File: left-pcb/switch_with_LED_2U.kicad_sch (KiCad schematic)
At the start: 3 parts, among them SW6 SW_SPST

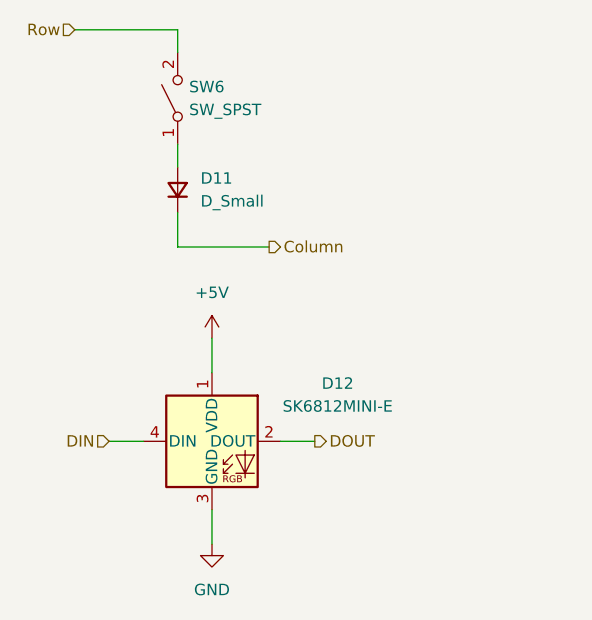
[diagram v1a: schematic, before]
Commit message: Initial modifications to reduce fab cost and add caps
Removing 1 row and column of keys, and majorly changing layout

Routing still in progress
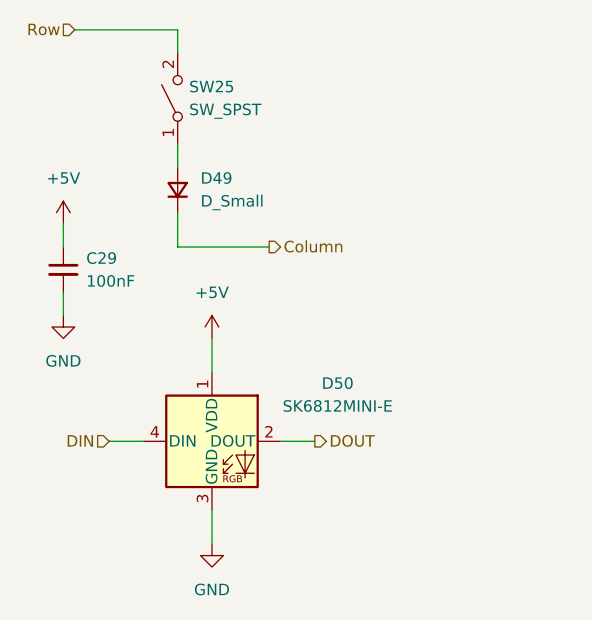
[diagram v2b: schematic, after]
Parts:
- removed D11: D_Small, Diode_SMD:D_SOD-123, symbol Device:D_Small
- removed D12: SK6812MINI-E, SW-Adafruit:LED_SK6812MINI-E_REVERSE_MOUNT_3.2x2.8mm_P1.09mm, symbol SW-Adafruit:SK6812MINI-E
- removed SW6: SW_SPST, PCM_Switch_Keyboard_Hotswap_Kailh:SW_Hotswap_Kailh_MX_2.00u, symbol Switch:SW_SPST
- added C29: 100nF, Capacitor_SMD:C_1206_3216Metric_Pad1.33x1.80mm_HandSolder, symbol Device:C_Small
- added D49: D_Small, Diode_SMD:D_SOD-123, symbol Device:D_Small
- added D50: SK6812MINI-E, SW-Adafruit:LED_SK6812MINI-E_REVERSE_MOUNT_3.2x2.8mm_P1.09mm, symbol SW-Adafruit:SK6812MINI-E
- added SW25: SW_SPST, PCM_Switch_Keyboard_Hotswap_Kailh:SW_Hotswap_Kailh_MX_2.00u, symbol Switch:SW_SPST
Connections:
- net +5V: now also C29.1, D50.1 (VDD)
- net Column: now also D49.1 (K)
- net DIN: now also D50.4 (DIN)
- net DOUT: now also D50.2 (DOUT)
- net GND: now also C29.2, D50.3 (GND)
- net Row: now also SW25.2 (B)
- new net: D49.2 (A), SW25.1 (A)

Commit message: Caps, shrunk board, added mounting holes
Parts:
- C29: footprint Capacitor_SMD:C_1206_3216Metric_Pad1.33x1.80mm_HandSolder -> Capacitor_SMD:C_0805_2012Metric_Pad1.18x1.45mm_HandSolder
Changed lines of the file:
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@@
 			)
 		)
-		(property "Footprint" "Capacitor_SMD:C_1206_3216Metric_Pad1.33x1.80mm_HandSolder"
+		(property "Footprint" "Capacitor_SMD:C_0805_2012Metric_Pad1.18x1.45mm_HandSolder"
 			(at 107.95 113.03 0)
 			(effects

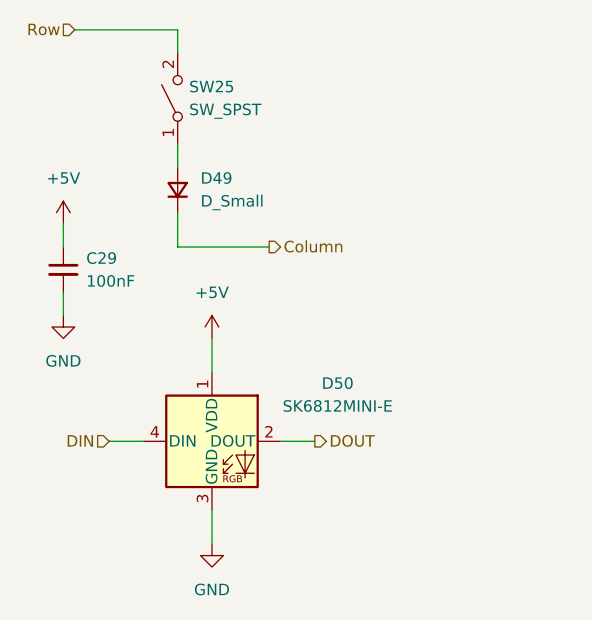
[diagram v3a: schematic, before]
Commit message: Adding values to Diodes and adding stabilizers to 2U switches
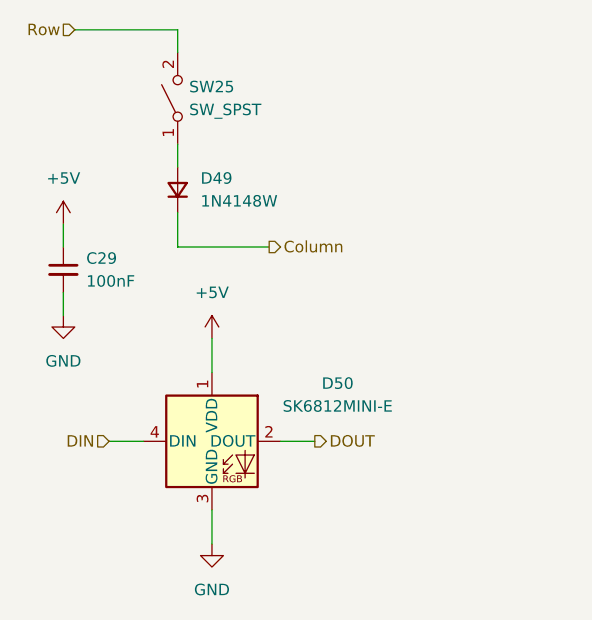
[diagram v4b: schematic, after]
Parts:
- D49: value D_Small -> 1N4148W
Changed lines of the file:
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@@
 			)
 		)
-		(property "Value" "D_Small"
+		(property "Value" "1N4148W"
 			(at 123.19 105.4099 90)
 			(effects

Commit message: Added extra column to left hand keyboard
Matching size to right hand side.
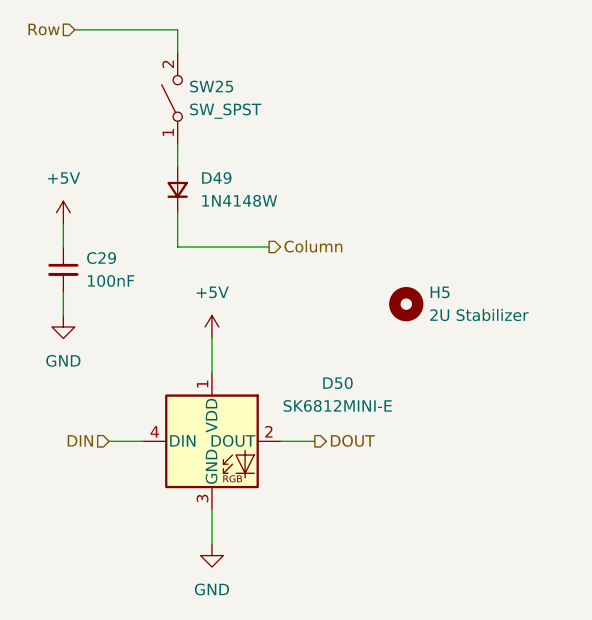
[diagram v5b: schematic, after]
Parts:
- added H5: 2U Stabilizer, PCM_Mounting_Keyboard_Stabilizer:Stabilizer_Cherry_MX_2.00u, symbol Mechanical:MountingHole
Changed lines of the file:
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@@
 		(dnp no)
 		(fields_autoplaced yes)
-		(property "Reference" "#PWR0113"
+		(property "Reference" "#PWR0114"
 			(at 107.95 124.46 0)
 			(effects
@@
 			(project "row_staggered_split_keyboard_left_side"
 				(path "/cf145565-22e2-4e5a-8a27-915862c57a1b/6b1ebd07-8927-4363-9ca1-15fd56b1bbda"
-					(reference "#PWR0113")
+					(reference "#PWR0114")
 					(unit 1)
 				)
@@
 		(dnp no)
 		(fields_autoplaced yes)
-		(property "Reference" "#PWR0114"
+		(property "Reference" "#PWR0115"
 			(at 124.46 124.46 0)
 			(effects
@@
 			(project "row_staggered_split_keyboard_left_side"
 				(path "/cf145565-22e2-4e5a-8a27-915862c57a1b/6b1ebd07-8927-4363-9ca1-15fd56b1bbda"
-					(reference "#PWR0114")
+					(reference "#PWR0115")
 					(unit 1)
 				)
@@
 		(dnp no)
 		(fields_autoplaced yes)
-		(property "Reference" "#PWR0115"
+		(property "Reference" "#PWR0116"
 			(at 124.46 149.86 0)
 			(effects
@@
 			(project "row_staggered_split_keyboard_left_side"
 				(path "/cf145565-22e2-4e5a-8a27-915862c57a1b/6b1ebd07-8927-4363-9ca1-15fd56b1bbda"
-					(reference "#PWR0115")
+					(reference "#PWR0116")
 					(unit 1)
 				)
@@
 	)
 	(symbol
+		(lib_id "Mechanical:MountingHole")
+		(at 146.05 116.84 0)
+		(unit 1)
+		(exclude_from_sim no)
+		(in_bom yes)
+		(on_board yes)
+		(dnp no)
+		(fields_autoplaced yes)
+		(property "Reference" "H5"
+			(at 148.59 115.5699 0)
+			(effects
+				(font
+					(size 1.27 1.27)
+				)
+				(justify left)
+			)
+		)
+		(property "Value" "2U Stabilizer"
+			(at 148.59 118.1099 0)
+			(effects
+				(font
+					(size 1.27 1.27)
+				)
+				(justify left)
+			)
+		)
+		(property "Footprint" "PCM_Mounting_Keyboard_Stabilizer:Stabilizer_Cherry_MX_2.00u"
+			(at 146.05 116.84 0)
+			(effects
+				(font
+					(size 1.27 1.27)
+				)
+				(hide yes)
+			)
+		)
+		(property "Datasheet" "~"
+			(at 146.05 116.84 0)
+			(effects
+				(font
+					(size 1.27 1.27)
+				)
+				(hide yes)
+			)
+		)
+		(property "Description" "Mounting Hole without connection"
+			(at 146.05 116.84 0)
+			(effects
+				(font
+					(size 1.27 1.27)
+				)
+				(hide yes)
+			)
+		)
+		(instances
+			(project ""
+				(path "/cf145565-22e2-4e5a-8a27-915862c57a1b/6b1ebd07-8927-4363-9ca1-15fd56b1bbda"
+					(reference "H5")
+					(unit 1)
+				)
+			)
+		)
+	)
+	(symbol
 		(lib_id "Device:C_Small")
 		(at 107.95 113.03 0)
@@
 		(dnp no)
 		(fields_autoplaced yes)
-		(property "Reference" "#PWR0112"
+		(property "Reference" "#PWR0113"
 			(at 107.95 111.76 0)
 			(effects
@@
 			(project "row_staggered_split_keyboard_left_side"
 				(path "/cf145565-22e2-4e5a-8a27-915862c57a1b/6b1ebd07-8927-4363-9ca1-15fd56b1bbda"
-					(reference "#PWR0112")
-					(unit 1)
-				)
+					(reference "#PWR0113")
+					(unit 1)
+				)

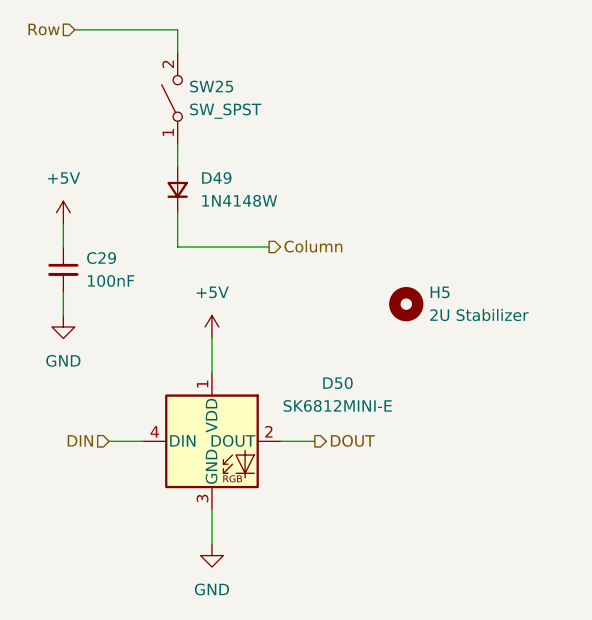
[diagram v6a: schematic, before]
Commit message: adding mounting hole in center for additional support, and cleaning up tracks/zones
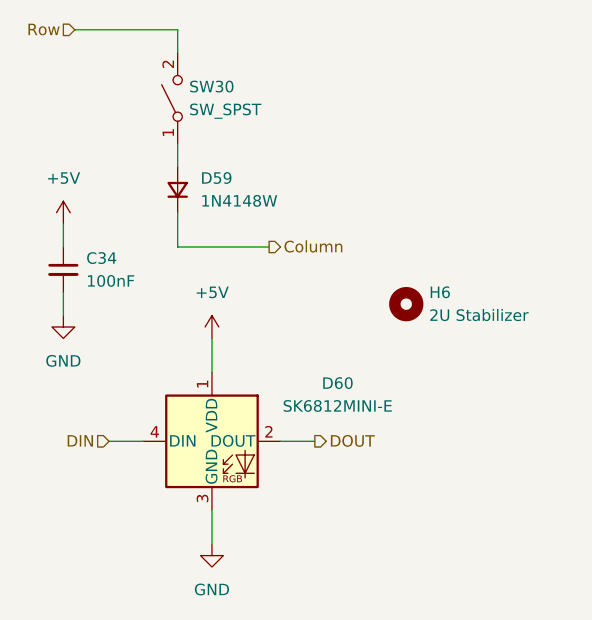
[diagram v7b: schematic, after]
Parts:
- renumbered C29 to C34, D49 to D59, D50 to D60, H5 to H6, SW25 to SW30
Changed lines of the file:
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@@
+	(wire
+		(pts
+			(xy 107.95 115.57) (xy 107.95 118.11)
+		)
+		(stroke
+			(width 0)
+			(type default)
+		)
+	)
+	(wire
+		(pts
+			(xy 113.03 132.08) (xy 116.84 132.08)
+		)
+		(stroke
+			(width 0)
+			(type default)
+		)
+	)
 	(wire
 		(pts
@@
 	(wire
 		(pts
-			(xy 107.95 115.57) (xy 107.95 118.11)
+			(xy 124.46 120.65) (xy 124.46 124.46)
+		)
+		(stroke
+			(width 0)
+			(type default)
+		)
+	)
+	(wire
+		(pts
+			(xy 107.95 107.95) (xy 107.95 110.49)
+		)
+		(stroke
+			(width 0)
+			(type default)
+		)
+	)
+	(wire
+		(pts
+			(xy 109.22 86.36) (xy 120.65 86.36)
+		)
+		(stroke
+			(width 0)
+			(type default)
+		)
+	)
+	(wire
+		(pts
+			(xy 120.65 106.68) (xy 120.65 110.49)
 		)
 		(stroke
@@
 	(wire
 		(pts
+			(xy 132.08 132.08) (xy 135.89 132.08)
+		)
+		(stroke
+			(width 0)
+			(type default)
+		)
+	)
+	(wire
+		(pts
 			(xy 120.65 99.06) (xy 120.65 101.6)
 		)
@@
 	(wire
 		(pts
-			(xy 132.08 132.08) (xy 135.89 132.08)
-		)
-		(stroke
-			(width 0)
-			(type default)
-		)
-	)
-	(wire
-		(pts
-			(xy 109.22 86.36) (xy 120.65 86.36)
-		)
-		(stroke
-			(width 0)
-			(type default)
-		)
-	)
-	(wire
-		(pts
-			(xy 113.03 132.08) (xy 116.84 132.08)
-		)
-		(stroke
-			(width 0)
-			(type default)
-		)
-	)
-	(wire
-		(pts
-			(xy 107.95 107.95) (xy 107.95 110.49)
-		)
-		(stroke
-			(width 0)
-			(type default)
-		)
-	)
-	(wire
-		(pts
 			(xy 124.46 139.7) (xy 124.46 143.51)
-		)
-		(stroke
-			(width 0)
-			(type default)
-		)
-	)
-	(wire
-		(pts
-			(xy 124.46 120.65) (xy 124.46 124.46)
-		)
-		(stroke
-			(width 0)
-			(type default)
-		)
-	)
-	(wire
-		(pts
-			(xy 120.65 106.68) (xy 120.65 110.49)
 		)
 		(stroke
@@
 		(dnp no)
 		(fields_autoplaced yes)
-		(property "Reference" "#PWR0114"
+		(property "Reference" "#PWR0134"
 			(at 107.95 124.46 0)
 			(hide yes)
@@
 			(project "row_staggered_split_keyboard_left_side"
 				(path "/cf145565-22e2-4e5a-8a27-915862c57a1b/6b1ebd07-8927-4363-9ca1-15fd56b1bbda"
-					(reference "#PWR0114")
+					(reference "#PWR0134")
 					(unit 1)
 				)
@@
 		(dnp no)
 		(fields_autoplaced yes)
-		(property "Reference" "#PWR0115"
+		(property "Reference" "#PWR0135"
 			(at 124.46 124.46 0)
 			(hide yes)
@@
 			(project "row_staggered_split_keyboard_left_side"
 				(path "/cf145565-22e2-4e5a-8a27-915862c57a1b/6b1ebd07-8927-4363-9ca1-15fd56b1bbda"
-					(reference "#PWR0115")
+					(reference "#PWR0135")
 					(unit 1)
 				)
@@
 		(dnp no)
 		(fields_autoplaced yes)
-		(property "Reference" "D49"
+		(property "Reference" "D59"
 			(at 123.19 102.8699 90)
 			(show_name no)
@@
 			(project "row_staggered_split_keyboard_left_side"
 				(path "/cf145565-22e2-4e5a-8a27-915862c57a1b/6b1ebd07-8927-4363-9ca1-15fd56b1bbda"
-					(reference "D49")
+					(reference "D59")
 					(unit 1)
 				)
@@
 		(dnp no)
 		(fields_autoplaced yes)
-		(property "Reference" "#PWR0116"
+		(property "Reference" "#PWR0136"
 			(at 124.46 149.86 0)
 			(hide yes)
@@
 			(project "row_staggered_split_keyboard_left_side"
 				(path "/cf145565-22e2-4e5a-8a27-915862c57a1b/6b1ebd07-8927-4363-9ca1-15fd56b1bbda"
-					(reference "#PWR0116")
+					(reference "#PWR0136")
 					(unit 1)
 				)
@@
 		(dnp no)
 		(fields_autoplaced yes)
-		(property "Reference" "SW25"
+		(property "Reference" "SW30"
 			(at 121.92 92.7099 90)
 			(show_name no)
@@
 			(project "row_staggered_split_keyboard_left_side"
 				(path "/cf145565-22e2-4e5a-8a27-915862c57a1b/6b1ebd07-8927-4363-9ca1-15fd56b1bbda"
-					(reference "SW25")
+					(reference "SW30")
 					(unit 1)
 				)
@@
 		(dnp no)
 		(fields_autoplaced yes)
-		(property "Reference" "H5"
+		(property "Reference" "H6"
 			(at 148.59 115.5699 0)
 			(show_name no)
@@
 			(project "row_staggered_split_keyboard_left_side"
 				(path "/cf145565-22e2-4e5a-8a27-915862c57a1b/6b1ebd07-8927-4363-9ca1-15fd56b1bbda"
-					(reference "H5")
+					(reference "H6")
 					(unit 1)
 				)
@@
 		(dnp no)
 		(fields_autoplaced yes)
-		(property "Reference" "C29"
+		(property "Reference" "C34"
 			(at 110.49 111.7662 0)
 			(show_name no)
@@
 			(project "row_staggered_split_keyboard_left_side"
 				(path "/cf145565-22e2-4e5a-8a27-915862c57a1b/6b1ebd07-8927-4363-9ca1-15fd56b1bbda"
-					(reference "C29")
+					(reference "C34")
 					(unit 1)
 				)
@@
 		(dnp no)
 		(fields_autoplaced yes)
-		(property "Reference" "#PWR0113"
+		(property "Reference" "#PWR0133"
 			(at 107.95 111.76 0)
 			(hide yes)
@@
 			(project "row_staggered_split_keyboard_left_side"
 				(path "/cf145565-22e2-4e5a-8a27-915862c57a1b/6b1ebd07-8927-4363-9ca1-15fd56b1bbda"
-					(reference "#PWR0113")
+					(reference "#PWR0133")
 					(unit 1)
 				)
@@
 		(dnp no)
 		(fields_autoplaced yes)
-		(property "Reference" "D50"
+		(property "Reference" "D60"
 			(at 138.43 125.6598 0)
 			(show_name no)
@@
 			(project "row_staggered_split_keyboard_left_side"
 				(path "/cf145565-22e2-4e5a-8a27-915862c57a1b/6b1ebd07-8927-4363-9ca1-15fd56b1bbda"
-					(reference "D50")
+					(reference "D60")
 					(unit 1)
 				)

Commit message: Boards were ordered
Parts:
- SW30: symbol Switch:SW_SPST -> SW-gElectroMech:SPST_MOM
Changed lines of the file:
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@@
 	)
 	(symbol
-		(lib_id "Switch:SW_SPST")
+		(lib_id "SW-gElectroMech:SPST_MOM")
 		(at 120.65 93.98 90)
 		(unit 1)
@@
 		)
 		(property "Datasheet" ""
-			(at 120.65 93.98 0)
+			(at 115.57 93.98 0)
 			(hide yes)
 			(show_name no)
@@
 			)
 		)
-		(property "Description" "Single Pole Single Throw (SPST) switch"
+		(property "Description" "Push button switch, generic, two pins"
 			(at 120.65 93.98 0)
 			(hide yes)
